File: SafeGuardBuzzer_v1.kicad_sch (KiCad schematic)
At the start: 16 parts, among them J1 SWD_DEBUG_PADS, J2 VBAT_RAW_GND_TEST_PADS, Q1 AO3400A logic-level NMOS, U1 DA14531MOD-00F01002

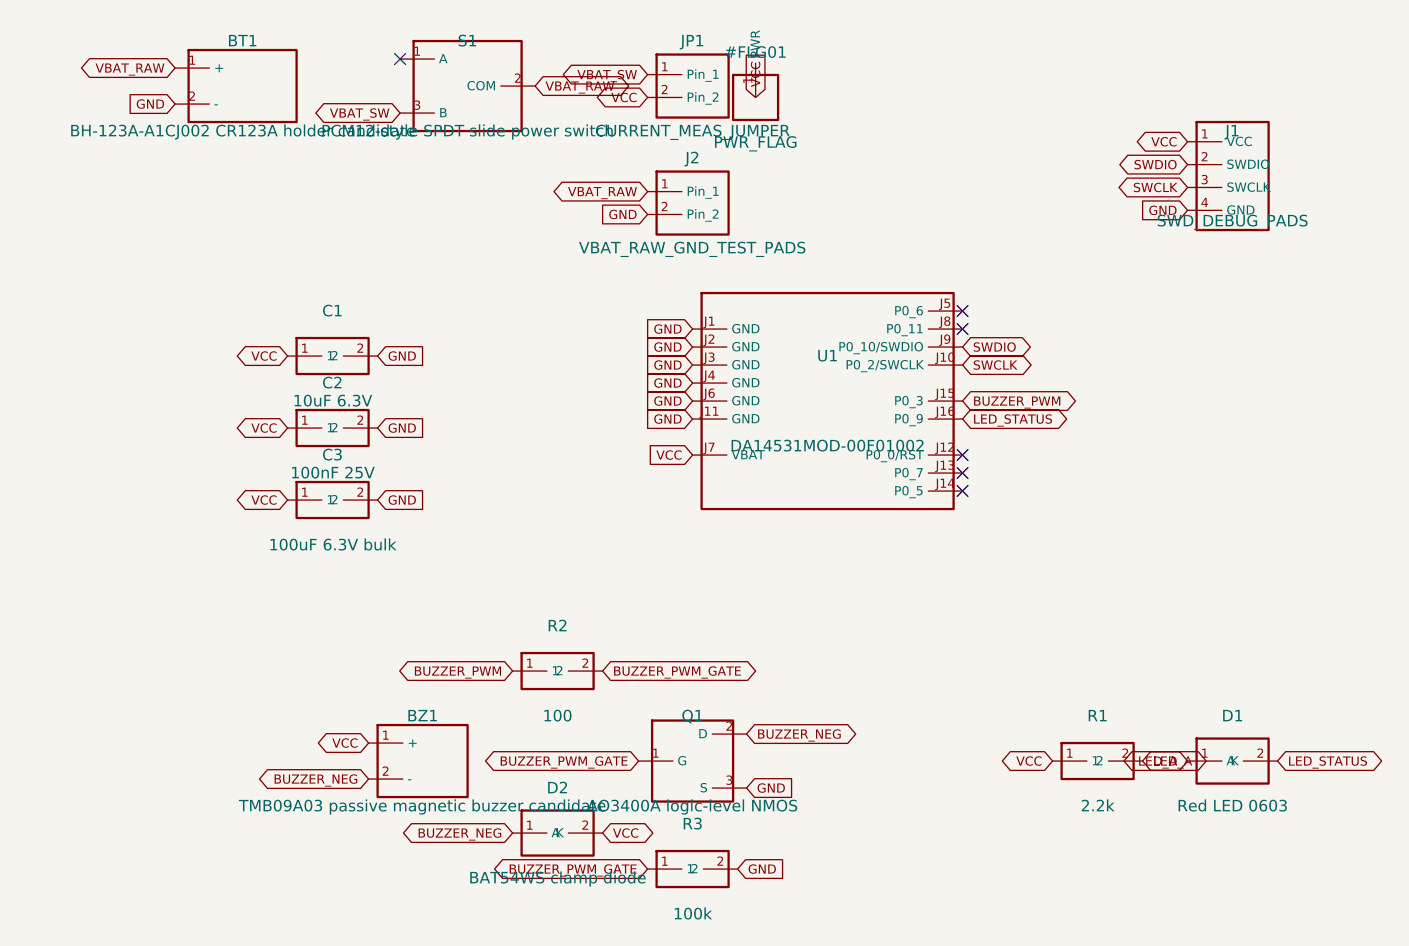
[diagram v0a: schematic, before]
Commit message: Resolve Buzzer CR123A holder footprint
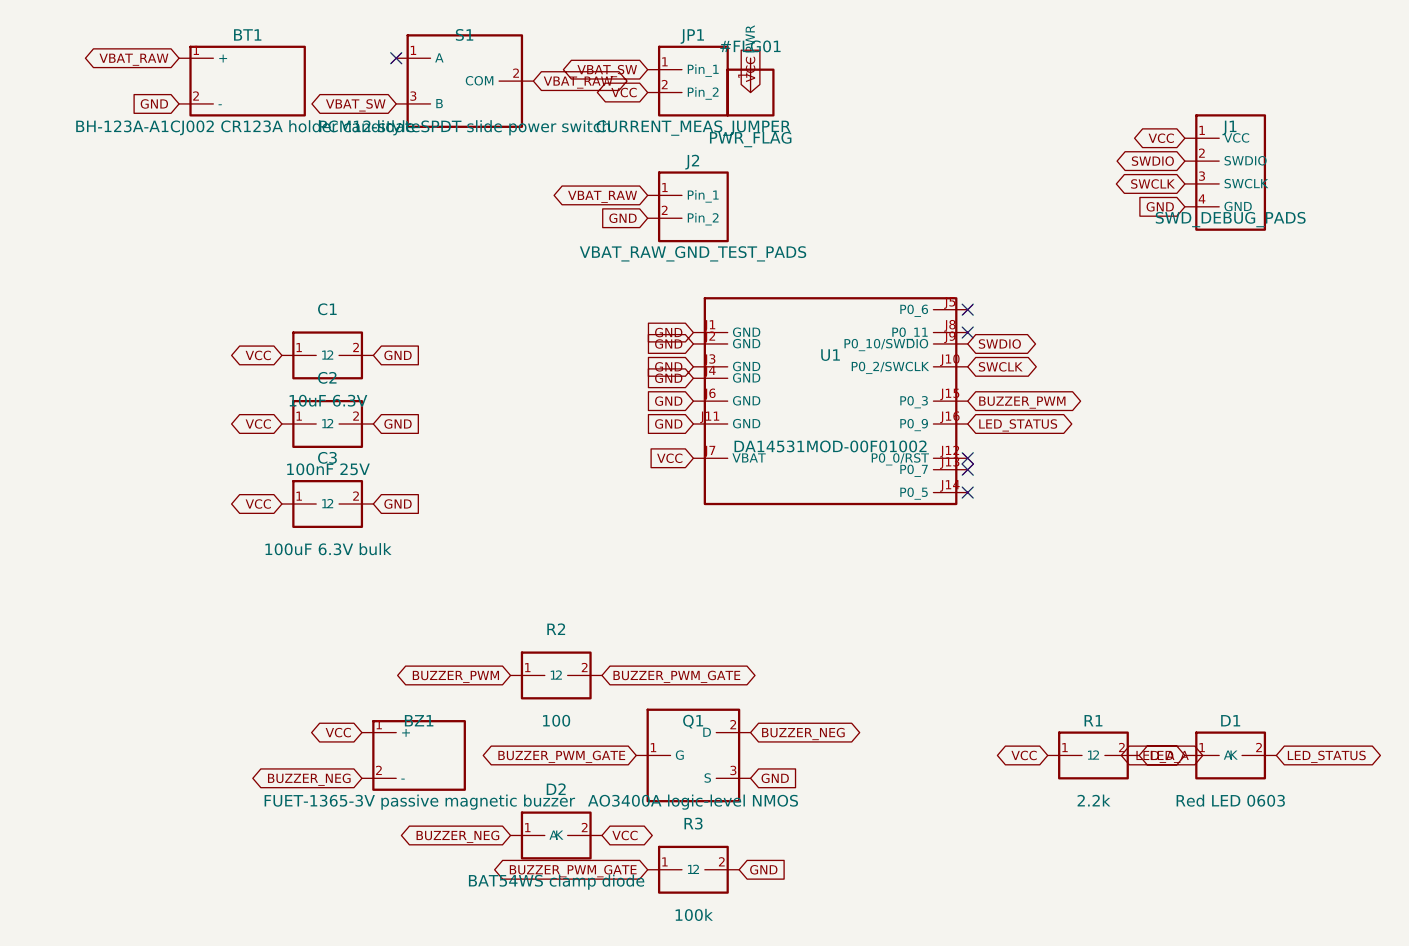
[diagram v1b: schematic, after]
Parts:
- BT1: footprint SafeGuardBuzzer_Local:BatteryHolder_CR123A_MYOUNG_BH-123A-A1CJ002_Candidate -> SafeGuardBuzzer_Local:BatteryHolder_CR123A_MYOUNG_BH-123A-A1CJ002_C5290177_THT
- BZ1: value TMB09A03 passive magnetic buzzer candidate -> FUET-1365-3V passive magnetic buzzer; footprint SafeGuardBuzzer_Local:Buzzer_TMB09A03_C49246938_Candidate -> SafeGuardBuzzer_Local:Buzzer_FUET_FUET-1365-3V_C417422; LCSC C49246938 -> C417422; MPN TMB09A03 -> FUET-1365-3V; Manufacturer (none) -> FUET / Fusheng Electronics
- J1: footprint SafeGuardBuzzer_Local:TP_SWD_1x04_1.27mm_Compact_Candidate -> SafeGuardBuzzer_Local:TP_SWD_1x04_1.27mm_Compact
- J2: footprint SafeGuardBuzzer_Local:TP_1x02_1.27mm_Compact_Candidate -> SafeGuardBuzzer_Local:TP_1x02_1.27mm_Compact
- JP1: footprint SafeGuardBuzzer_Local:TP_Current_Jumper_2Pad_Compact_Candidate -> SafeGuardBuzzer_Local:TP_Current_Jumper_2Pad_Compact
- U1: footprint SafeGuardBuzzer_Local:XCVR_DA14531MOD-00F01002_Candidate -> SafeGuardBuzzer_Local:XCVR_DA14531MOD-00F01002
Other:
- moved on the sheet: BT1, BZ1, C1, C2, C3, D1, JP1, R1, R2, S1
